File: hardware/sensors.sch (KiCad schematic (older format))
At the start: 25 parts, among them U1 LM358, U2 LAH-100P, U3 LOC110, U4 MCP6001, U5 ADA4805-1, U6 MCP6001

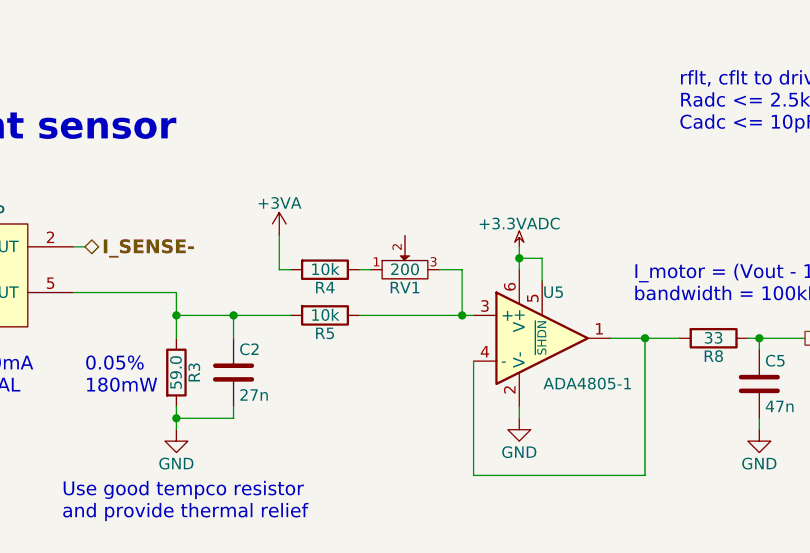
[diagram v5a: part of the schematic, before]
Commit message: Bulk cap layout, diodes, lugs, leds, trimpots
- Moved H-bridge bulk capacitors to horizontal layout
- Changed H-bridge and fan diodes to 100V schottky
- Made 4AWG lug mount footprint, added lugs to BOM
- Tweaked LED resistor values, added LEDs to BOM
- Made trimpot footprint, added trimpots to BOM
- Added snubber to ferrite bead circuit; also added FB to BOM
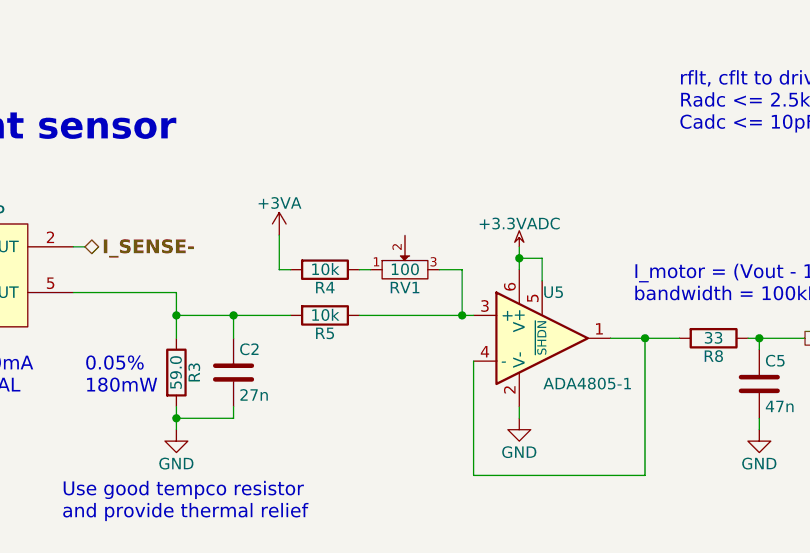
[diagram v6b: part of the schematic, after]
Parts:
- RV1: value 200 -> 100; footprint (none) -> 2kwMotorController:Trimpot-23B
- RV2: footprint (none) -> 2kwMotorController:Trimpot-23B
- U3: footprint Housings_DIP:DIP-8_W7.62mm -> SMD_Packages:DIP-8_SMD
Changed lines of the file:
@@
 $EndComp
 $Comp
-L GND #PWR01
+L GND #PWR8
 U 1 1 5975C471
 P 3150 2700
-F 0 "#PWR01" H 3150 2450 50  0001 C CNN
+F 0 "#PWR8" H 3150 2450 50  0001 C CNN
 F 1 "GND" H 3150 2550 50  0000 C CNN
 F 2 "" H 3150 2700 50  0000 C CNN
@@
 $EndComp
 $Comp
-L GND #PWR02
+L GND #PWR14
 U 1 1 5975C76F
 P 4650 2650
-F 0 "#PWR02" H 4650 2400 50  0001 C CNN
+F 0 "#PWR14" H 4650 2400 50  0001 C CNN
 F 1 "GND" H 4650 2500 50  0000 C CNN
 F 2 "" H 4650 2650 50  0000 C CNN
@@
 bus voltage sensor
 $Comp
-L +9V #PWR03
+L +9V #PWR17
 U 1 1 597CF4DC
 P 8450 5400
-F 0 "#PWR03" H 8450 5250 50  0001 C CNN
+F 0 "#PWR17" H 8450 5250 50  0001 C CNN
 F 1 "+9V" H 8450 5540 50  0000 C CNN
 F 2 "" H 8450 5400 50  0000 C CNN
@@
 F 0 "U3" H 3250 6000 60  0000 C CNN
 F 1 "LOC110" H 3250 6500 60  0000 C CNN
-F 2 "Housings_DIP:DIP-8_W7.62mm" H 3400 6050 60  0001 C CNN
+F 2 "SMD_Packages:DIP-8_SMD" H 3400 6050 60  0001 C CNN
 F 3 "" H 3400 6050 60  0000 C CNN
 	1    3250 6250
@@
 $EndComp
 $Comp
-L GND #PWR04
+L GND #PWR3
 U 1 1 597E9194
 P 1650 6100
-F 0 "#PWR04" H 1650 5850 50  0001 C CNN
+F 0 "#PWR3" H 1650 5850 50  0001 C CNN
 F 1 "GND" H 1650 5950 50  0000 C CNN
 F 2 "" H 1650 6100 50  0000 C CNN
@@
 $EndComp
 $Comp
-L GND #PWR05
+L GND #PWR12
 U 1 1 597EB09C
 P 4050 6550
-F 0 "#PWR05" H 4050 6300 50  0001 C CNN
+F 0 "#PWR12" H 4050 6300 50  0001 C CNN
 F 1 "GND" H 4050 6400 50  0000 C CNN
 F 2 "" H 4050 6550 50  0000 C CNN
@@
 $EndComp
 $Comp
-L +12V_ISO #PWR06
+L +12V_ISO #PWR4
 U 1 1 59A951A8
 P 1950 5850
-F 0 "#PWR06" H 1950 5700 50  0001 C CNN
+F 0 "#PWR4" H 1950 5700 50  0001 C CNN
 F 1 "+12V_ISO" H 1950 5990 50  0000 C CNN
 F 2 "" H 1950 5850 50  0000 C CNN
@@
 VBUS
 $Comp
-L +12V_ISO #PWR07
+L +12V_ISO #PWR6
 U 1 1 59A9895F
 P 2800 5850
-F 0 "#PWR07" H 2800 5700 50  0001 C CNN
+F 0 "#PWR6" H 2800 5700 50  0001 C CNN
 F 1 "+12V_ISO" H 2800 5990 50  0000 C CNN
 F 2 "" H 2800 5850 50  0000 C CNN
@@
 $EndComp
 $Comp
-L +12V #PWR08
+L +12V #PWR1
 U 1 1 59A9BD78
 P 850 2000
-F 0 "#PWR08" H 850 1850 50  0001 C CNN
+F 0 "#PWR1" H 850 1850 50  0001 C CNN
 F 1 "+12V" H 850 2140 50  0000 C CNN
 F 2 "" H 850 2000 50  0000 C CNN
@@
 	2700 1900 2750 1900
 $Comp
-L GND #PWR09
+L GND #PWR10
 U 1 1 599BDED6
 P 3800 6550
-F 0 "#PWR09" H 3800 6300 50  0001 C CNN
+F 0 "#PWR10" H 3800 6300 50  0001 C CNN
 F 1 "GND" H 3800 6400 50  0000 C CNN
 F 2 "" H 3800 6550 50  0000 C CNN
@@
 F 0 "RV2" H 4400 5620 50  0000 C CNN
 F 1 "36k" H 4400 5700 50  0000 C CNN
-F 2 "" H 4400 5700 50  0001 C CNN
+F 2 "2kwMotorController:Trimpot-23B" H 4400 5700 50  0001 C CNN
 F 3 "" H 4400 5700 50  0000 C CNN
 	1    4400 5700
@@
 Connection ~ 4600 5700
 $Comp
-L +3.3VADC #PWR010
+L +3.3VADC #PWR13
 U 1 1 59A58825
 P 4650 1900
-F 0 "#PWR010" H 4800 1850 50  0001 C CNN
+F 0 "#PWR13" H 4800 1850 50  0001 C CNN
 F 1 "+3.3VADC" H 4650 2000 50  0000 C CNN
 F 2 "" H 4650 1900 50  0000 C CNN
@@
 $EndComp
 $Comp
-L +3.3VADC #PWR011
+L +3.3VADC #PWR11
 U 1 1 59A58E4C
 P 4050 5850
-F 0 "#PWR011" H 4200 5800 50  0001 C CNN
+F 0 "#PWR11" H 4200 5800 50  0001 C CNN
 F 1 "+3.3VADC" H 4050 5950 50  0000 C CNN
 F 2 "" H 4050 5850 50  0000 C CNN
@@
 $EndComp
 $Comp
-L +3.3VADC #PWR012
+L +3.3VADC #PWR19
 U 1 1 59A59C83
 P 9000 5400
-F 0 "#PWR012" H 9150 5350 50  0001 C CNN
+F 0 "#PWR19" H 9150 5350 50  0001 C CNN
 F 1 "+3.3VADC" H 9000 5500 50  0000 C CNN
 F 2 "" H 9000 5400 50  0000 C CNN
@@
 P 4150 2000
 F 0 "RV1" H 4150 1920 50  0000 C CNN
-F 1 "200" H 4150 2000 50  0000 C CNN
-F 2 "" H 4150 2000 50  0001 C CNN
+F 1 "100" H 4150 2000 50  0000 C CNN
+F 2 "2kwMotorController:Trimpot-23B" H 4150 2000 50  0001 C CNN
 F 3 "" H 4150 2000 50  0000 C CNN
 	1    4150 2000
@@
 0.05%\n180mW
 $Comp
-L +3VA #PWR013
+L +3VA #PWR9
 U 1 1 59C015DC
 P 3600 1850
-F 0 "#PWR013" H 3600 1700 50  0001 C CNN
+F 0 "#PWR9" H 3600 1700 50  0001 C CNN
 F 1 "+3VA" H 3600 1990 50  0000 C CNN
 F 2 "" H 3600 1850 50  0000 C CNN
@@
 $EndComp
 $Comp
-L GNDPWR #PWR014
+L GNDPWR #PWR7
 U 1 1 59C067BD
 P 2900 6500
-F 0 "#PWR014" H 2900 6300 50  0001 C CNN
+F 0 "#PWR7" H 2900 6300 50  0001 C CNN
 F 1 "GNDPWR" H 2900 6370 50  0000 C CNN
 F 2 "" H 2900 6450 50  0000 C CNN
@@
 $EndComp
 $Comp
-L GNDPWR #PWR015
+L GNDPWR #PWR5
 U 1 1 59C0683C
 P 1950 6550
-F 0 "#PWR015" H 1950 6350 50  0001 C CNN
+F 0 "#PWR5" H 1950 6350 50  0001 C CNN
 F 1 "GNDPWR" H 1950 6420 50  0000 C CNN
 F 2 "" H 1950 6500 50  0000 C CNN
@@
 $EndComp
 $Comp
-L GND #PWR016
+L GND #PWR18
 U 1 1 59C0EF65
 P 8450 6250
-F 0 "#PWR016" H 8450 6000 50  0001 C CNN
+F 0 "#PWR18" H 8450 6000 50  0001 C CNN
 F 1 "GND" H 8450 6100 50  0000 C CNN
 F 2 "" H 8450 6250 50  0000 C CNN
@@
 $EndComp
 $Comp
-L GND #PWR017
+L GND #PWR20
 U 1 1 59C0EFCE
 P 9000 6100
-F 0 "#PWR017" H 9000 5850 50  0001 C CNN
+F 0 "#PWR20" H 9000 5850 50  0001 C CNN
 F 1 "GND" H 9000 5950 50  0000 C CNN
 F 2 "" H 9000 6100 50  0000 C CNN
@@
 	5700 2650 5700 2700
 $Comp
-L GND #PWR018
+L GND #PWR16
 U 1 1 59B94DC3
 P 5700 2700
-F 0 "#PWR018" H 5700 2450 50  0001 C CNN
+F 0 "#PWR16" H 5700 2450 50  0001 C CNN
 F 1 "GND" H 5700 2550 50  0000 C CNN
 F 2 "" H 5700 2700 50  0000 C CNN
@@
 $EndComp
 $Comp
-L GND #PWR019
+L GND #PWR15
 U 1 1 59B99145
 P 5100 6600
-F 0 "#PWR019" H 5100 6350 50  0001 C CNN
+F 0 "#PWR15" H 5100 6350 50  0001 C CNN
 F 1 "GND" H 5100 6450 50  0000 C CNN
 F 2 "" H 5100 6600 50  0000 C CNN
@@
 $EndComp
 $Comp
-L GND #PWR020
+L GND #PWR21
 U 1 1 59B9CA89
 P 10050 6150
-F 0 "#PWR020" H 10050 5900 50  0001 C CNN
+F 0 "#PWR21" H 10050 5900 50  0001 C CNN
 F 1 "GND" H 10050 6000 50  0000 C CNN
 F 2 "" H 10050 6150 50  0000 C CNN

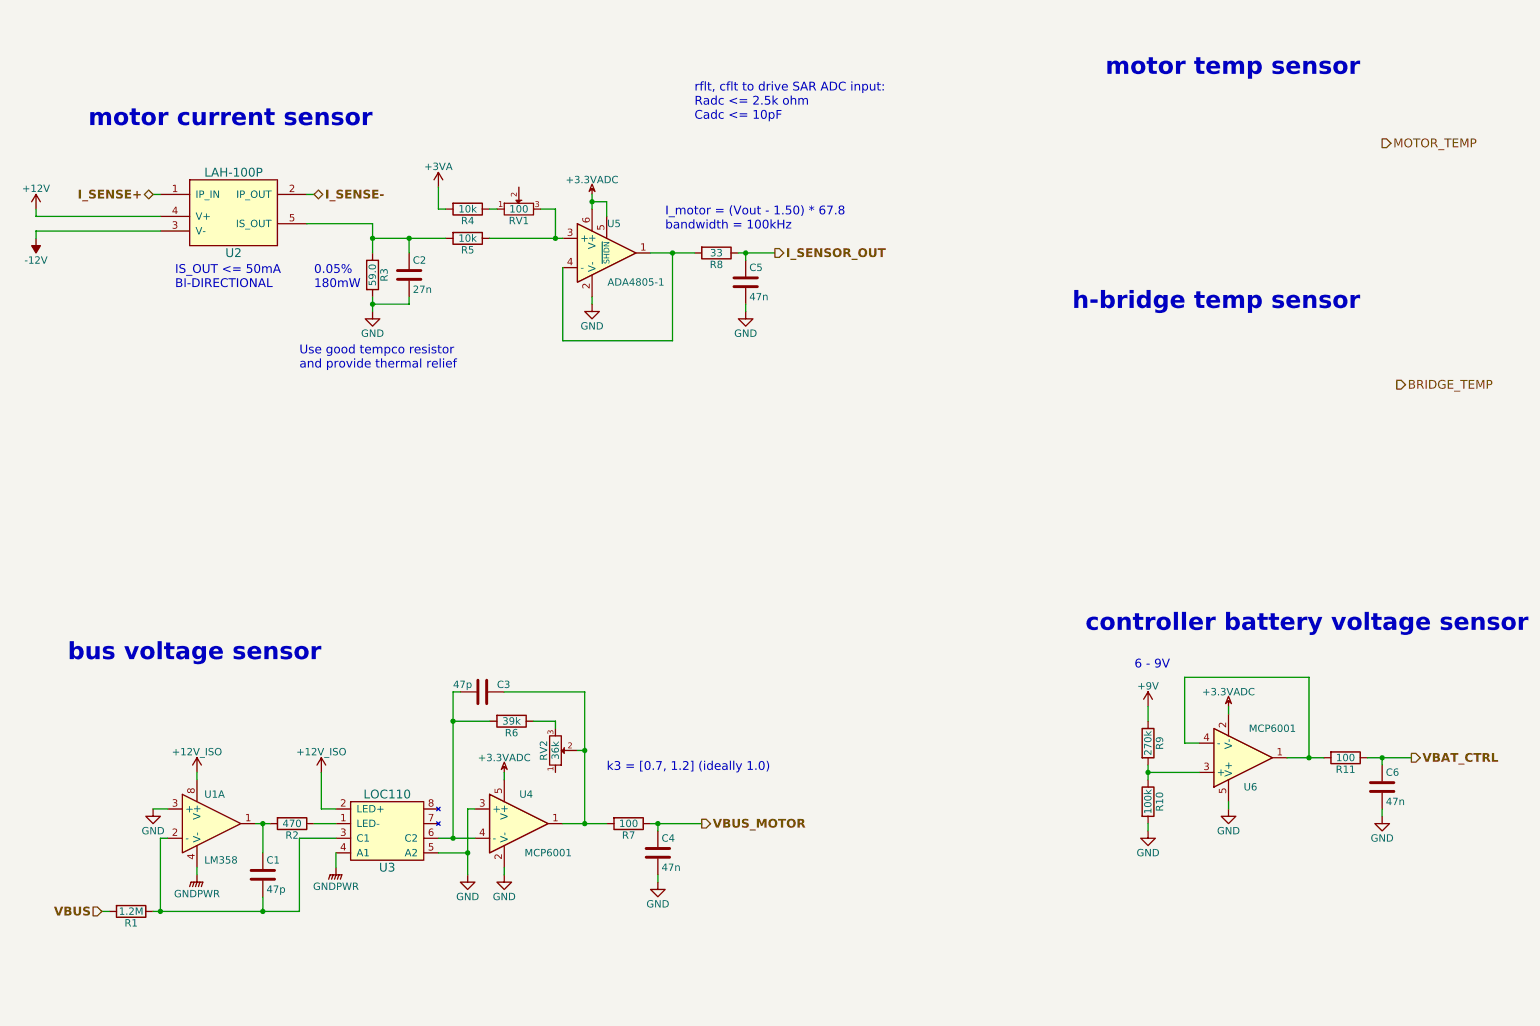
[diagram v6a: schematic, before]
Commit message: Inrush circuit, mounting hole position, temp sensor
- Split inrush circuit (one for each bulk cap). Replaced NTC
  thermistor with 2W power resistor. Replaced D2Pak MOSFET with
  LFPAK MOSFETs.
- Approximate position of mechanical holes chosen.
- Added thermistor temp sensor circuits.
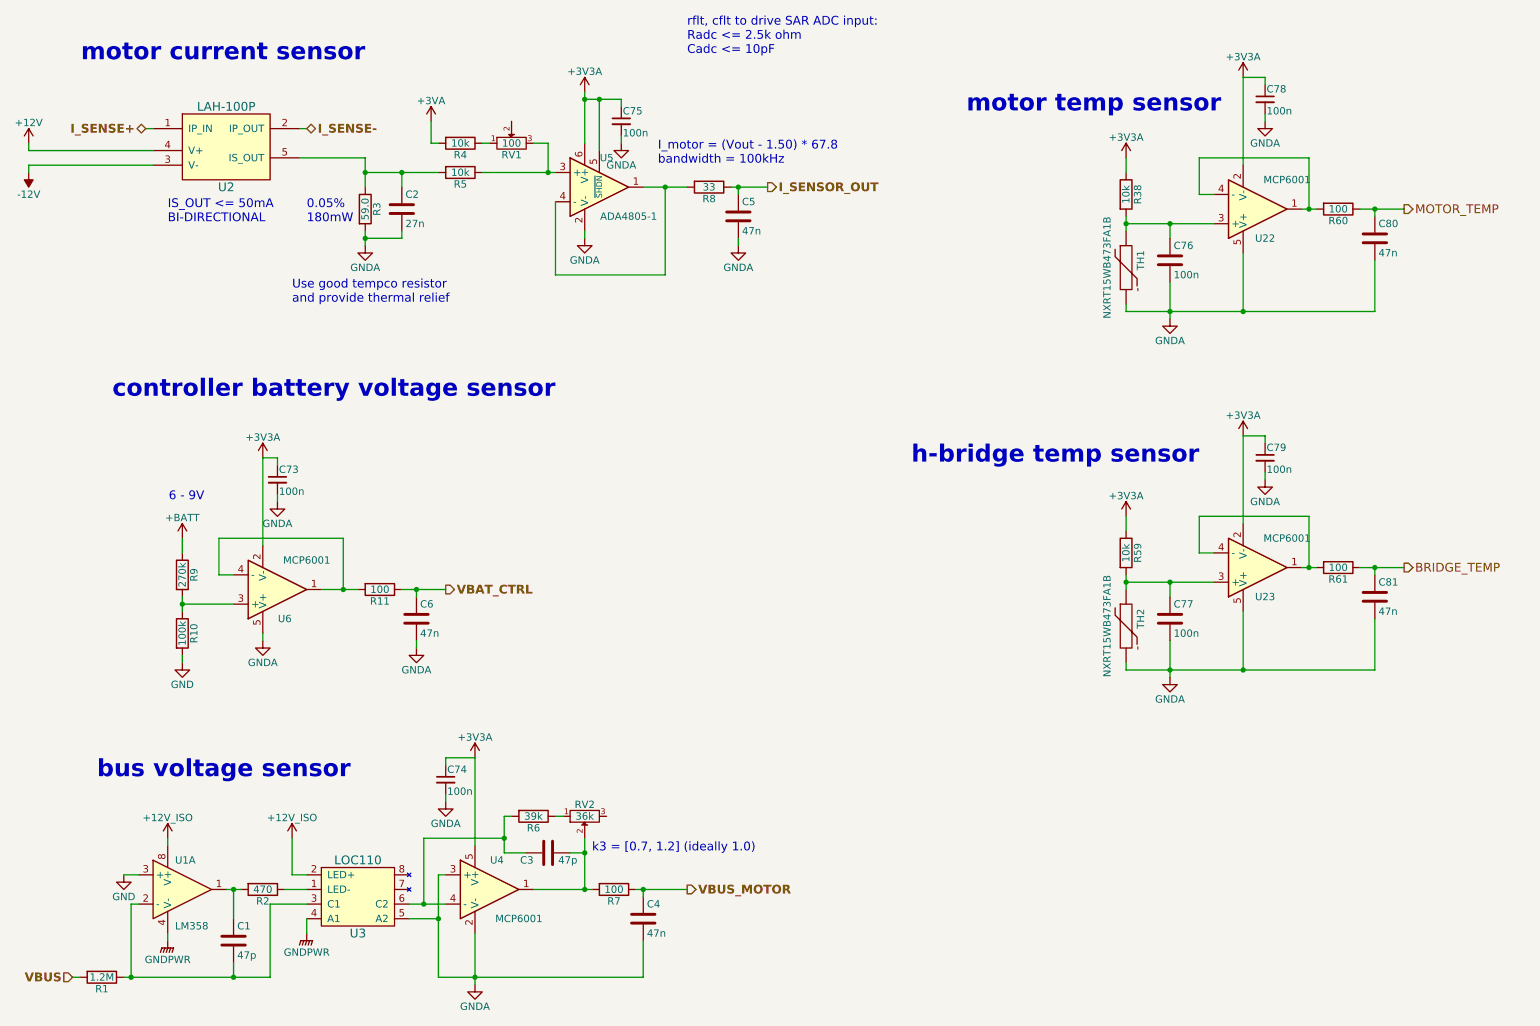
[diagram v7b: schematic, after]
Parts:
- added C73, C74, C75, C78, C79: 100n, Capacitors_SMD:C_0603, symbol C_Small
- added C76, C77: 100n, Capacitors_SMD:C_0603, symbol C
- added C80, C81: 47n, Capacitors_SMD:C_0603, symbol C
- added R38, R59: 10k, Resistors_SMD:R_0603, symbol R
- added R60, R61: 100, Resistors_SMD:R_0603, symbol R
- added TH1, TH2: NXRT15WB473FA1B, symbol THERMISTOR
- added U22, U23: MCP6001, TO_SOT_Packages_SMD:SC-70-5, symbol MCP6001
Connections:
- net +3.3VADC is gone; now on net +3V3: U4.5 (V+), U5.5 (~SHDN), U5.6 (V+), U6.2 (V-)
- net +3V3: now also C73.1, C74.1, C75.1, C78.1, C79.1, R38.1, R59.1, U22.2 (V-), U23.2 (V-)
- net BRIDGE_TEMP: now also C81.1, R61.1
- net GND: no longer C2.2, C4.2, C5.2, C6.2, R3.2, U3.5 (A2), U4.2 (V-), U4.3 (+), U5.2 (V-), U6.5 (V+)
- net MOTOR_TEMP: now also C80.1, R60.1
- net at R6.2, U3.6 (C2), U4.4 (-): now also C3.1; no longer C3.2
- net at R7.2, RV2.2, U4.1: now also C3.2; no longer C3.1
- net at R6.1: now also RV2.1; no longer RV2.3
- net +9V renamed +BATT
- new net: C76.1, R38.2, TH1.1, U22.3 (+)
- new net: R60.2, U22.1, U22.4 (-)
- new net: C77.1, R59.2, TH2.1, U23.3 (+)
- new net: R61.2, U23.1, U23.4 (-)
- new net GNDA: C2.2, C4.2, C5.2, C6.2, C73.2, C74.2, C75.2, C76.2, C77.2, C78.2, C79.2, C80.2, C81.2, R3.2, TH1.2, TH2.2, U22.5 (V+), U23.5 (V+), U3.5 (A2), U4.2 (V-), U4.3 (+), U5.2 (V-), U6.5 (V+)
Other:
- moved on the sheet: C1, C2, C3, C4, C5, C6, R1, R10, R11, R2, R3, R4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

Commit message: High amp routes, sensors
- Adjusted high current routing to improve clearances. Recommend
  3mm high busbar to compensate for reduced busbar width to 2mm.
- Shrank TO-247 pads by 1mm (lengthwise) to improve busbar clearance.
- Removed unecessary buffers / SAR ADC drive circuits from low-bandwidth
  sensors.
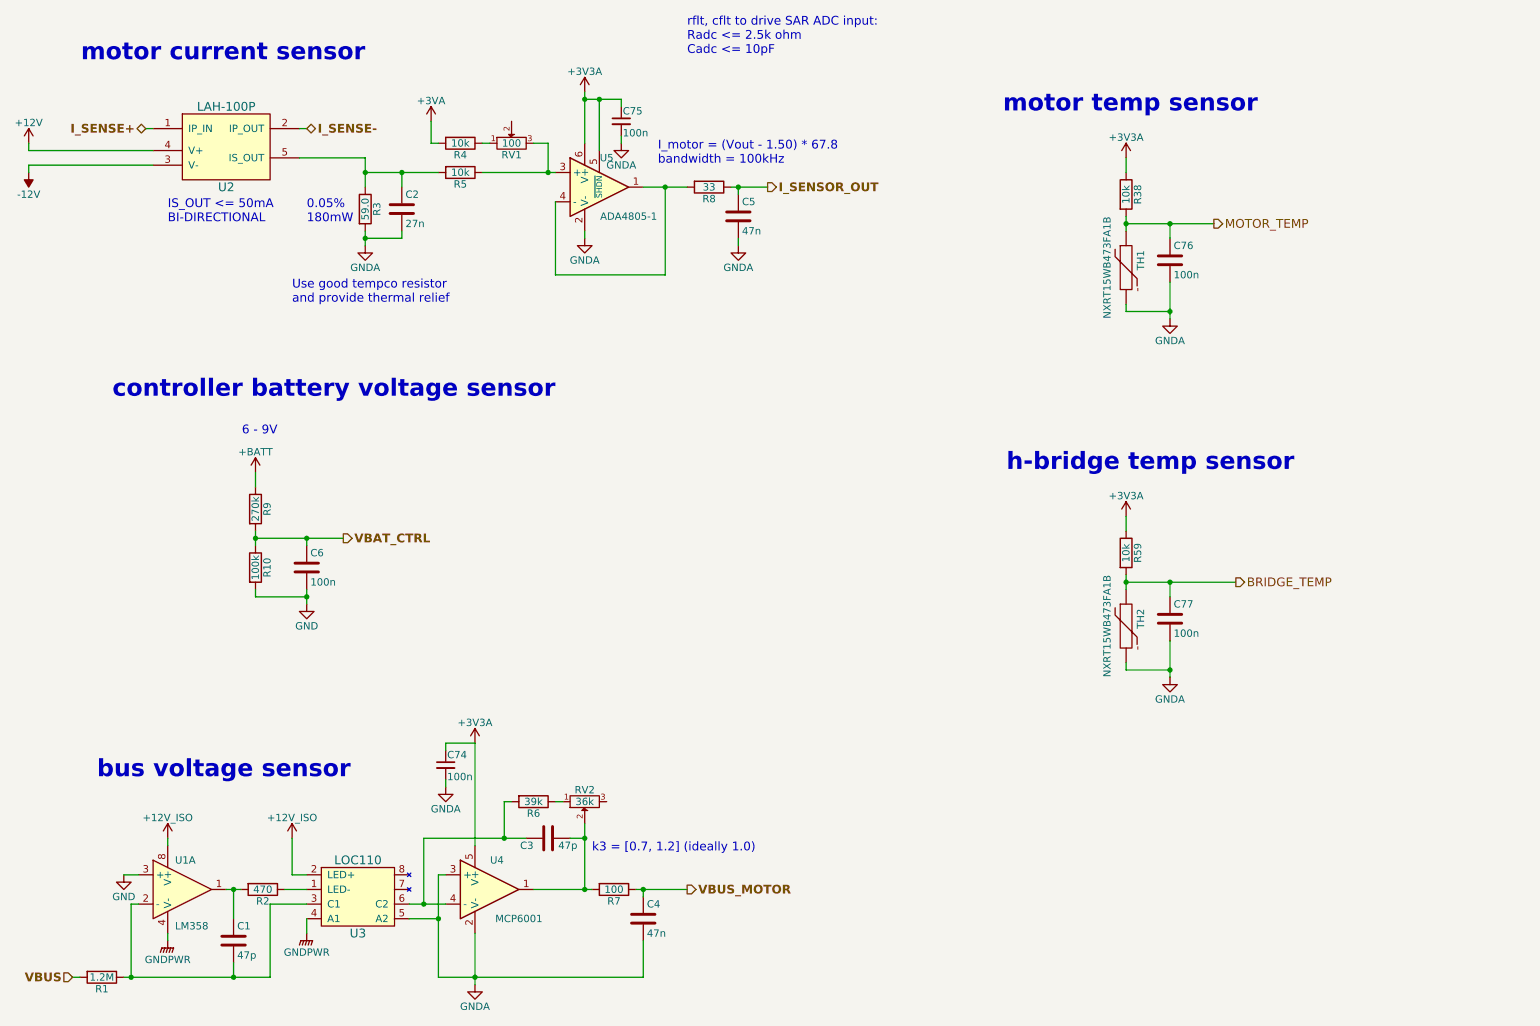
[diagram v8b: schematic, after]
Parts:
- removed C73, C78, C79: 100n, Capacitors_SMD:C_0603, symbol C_Small
- removed C80, C81: 47n, Capacitors_SMD:C_0603, symbol C
- removed R11, R60, R61: 100, Resistors_SMD:R_0603, symbol R
- removed U22, U23, U6: MCP6001, TO_SOT_Packages_SMD:SC-70-5, symbol MCP6001
- C6: value 47n -> 100n
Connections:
- net BRIDGE_TEMP: now also C77.1, R59.2, TH2.1
- net GND: now also C6.2
- net GNDA: no longer C6.2
- net MOTOR_TEMP: now also C76.1, R38.2, TH1.1
- net VBAT_CTRL: now also R10.1, R9.2
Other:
- moved on the sheet: C3, C74, R10, R6, R9, RV2
